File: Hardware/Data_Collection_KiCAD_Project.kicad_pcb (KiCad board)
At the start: 4 copper layers, 80 x 93.2 mm, 59 parts, among them IC1 STM32L562VET6Q, J1 10118192-0001LF, J2 Conn_Coaxial, J3 L717SDC37P1ACH4F, J4 I2C1 Debug, J6 UART Debug, J7 SPI 1 Debug, Q1 SI1040X-T1-GE3, U1 LM317T, U2 KX134-1211, U3 MCP9808_MSOP, U4 MAX-8Q, U5 USBLC6-2SC6, U6 W25Q32JVSS, U7 MS5607-02BA, U8 BNO055, Y1 32MHz, Y2 32.768kHz

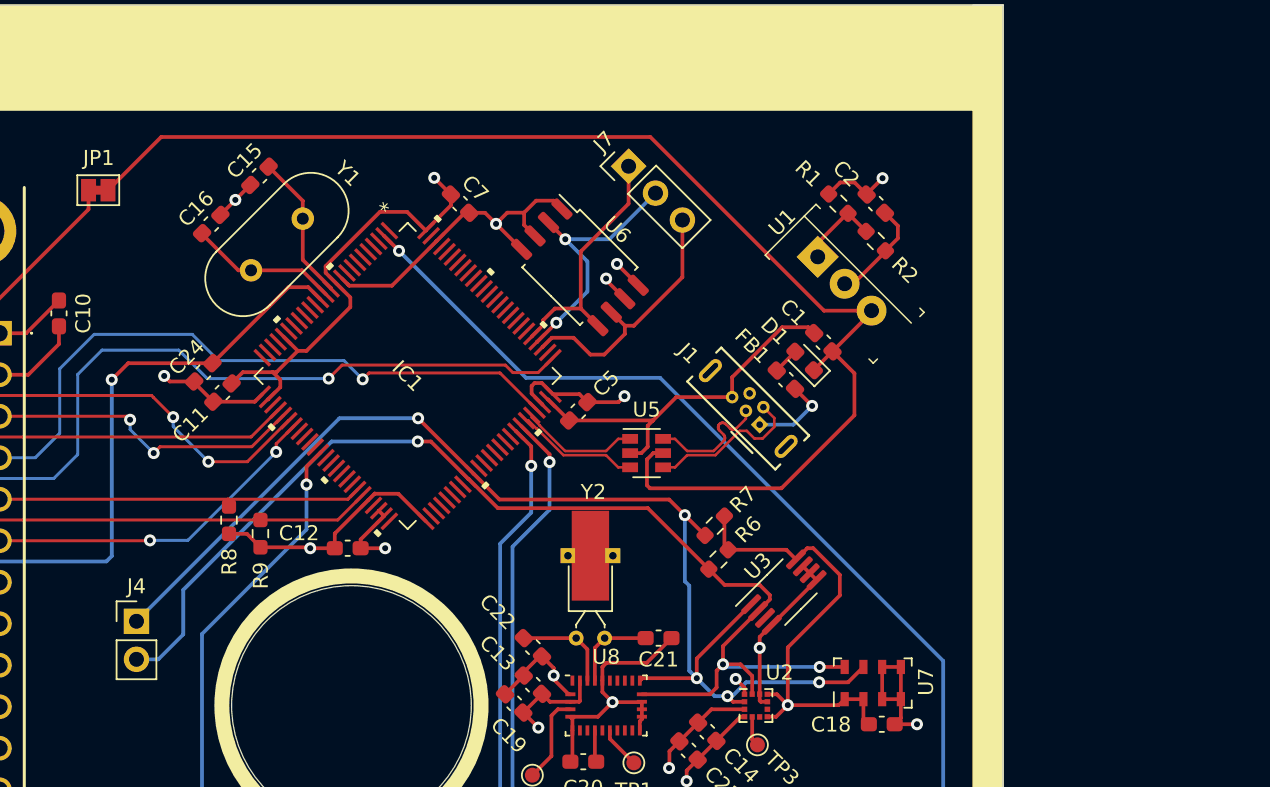
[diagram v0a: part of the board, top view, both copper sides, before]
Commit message: Updated MCU Component Sheet
Used the file from the Telemetry board for compatibility and commonality.
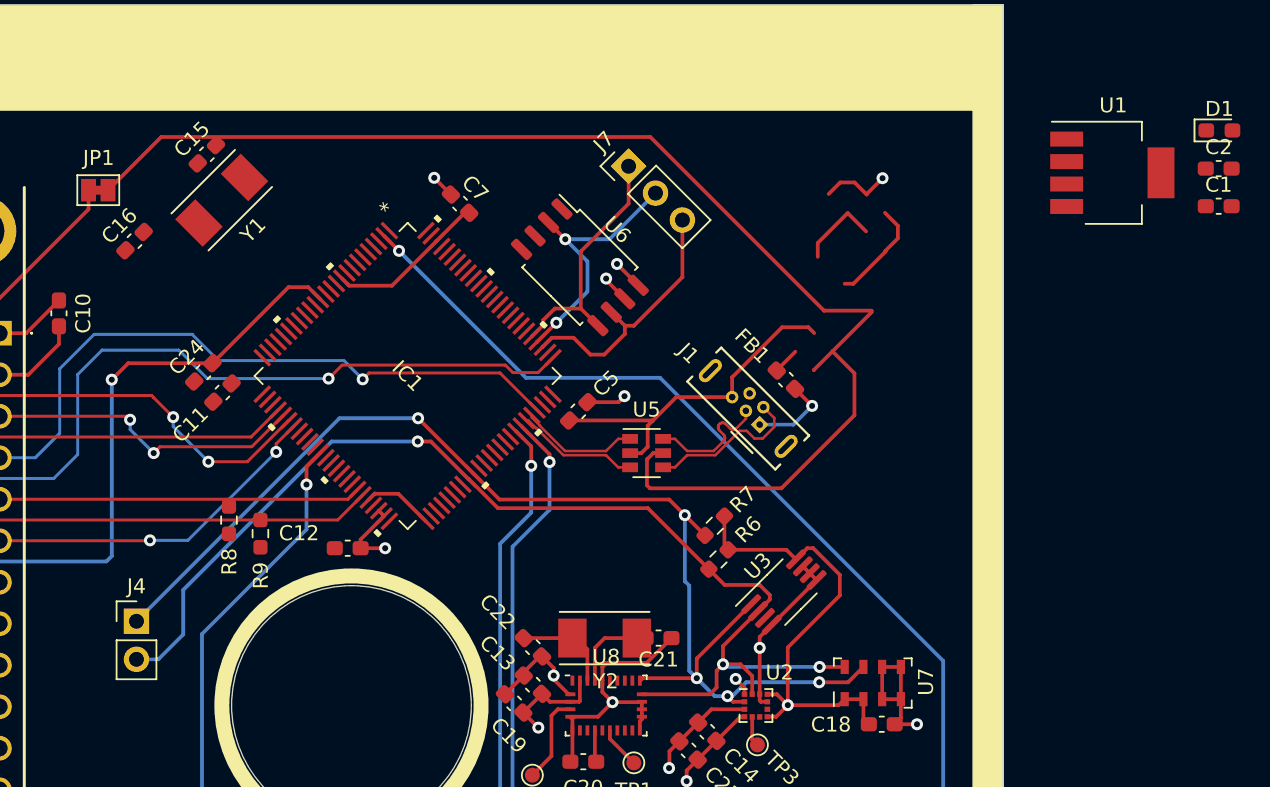
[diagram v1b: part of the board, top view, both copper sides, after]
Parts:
- removed R1: 390, Resistor_SMD:R_0603_1608Metric_Pad0.98x0.95mm_HandSolder
- removed R2: 240, Resistor_SMD:R_0603_1608Metric_Pad0.98x0.95mm_HandSolder
- D1: value D_Schottky -> D_Schottky_Small
- U1: value LM317T -> LP38692MPX-ADJ; footprint digikey-footprints:TO-220-3 -> Package_TO_SOT_SMD:SOT-223-5
- Y1: footprint Crystal:Crystal_HC49-4H_Vertical -> RDT_Custom_Footprints:XTAL_ABM7-32.000MHZ-D2Y-T
- Y2: footprint Crystal:Crystal_DS26_D2.0mm_L6.0mm_Horizontal_1EP_style2 -> RDT_Custom_Footprints:XTAL_ABM7-32.000MHZ-D2Y-T
- moved D1 31.7 mm to (174.4, 60.1), turned to 0 degrees
- moved C1 27.9 mm to (174.4, 65.1), turned to 0 degrees
- moved C2 23.0 mm to (174.4, 62.6), turned to 0 degrees
- moved U1 20.4 mm to (167.3, 62.9), turned to 0 degrees
- moved Y1 5.55 mm to (107.8, 64.7)
- moved C16 5.25 mm to (102.0, 67.5)
- moved C15 3.79 mm to (106.8, 61.7)
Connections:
- C2 pad 1: +3V3 -> Net-(C2-Pad1)
- IC1 pad 1: (no net) -> unconnected-(IC1-Pad1)
- IC1 pad 15: (no net) -> unconnected-(IC1-Pad15)
- IC1 pad 16: (no net) -> unconnected-(IC1-Pad16)
- IC1 pad 17: (no net) -> unconnected-(IC1-Pad17)
- IC1 pad 18: (no net) -> unconnected-(IC1-Pad18)
- IC1 pad 19: (no net) -> unconnected-(IC1-Pad19)
- IC1 pad 20: (no net) -> unconnected-(IC1-Pad20)
- IC1 pad 22: (no net) -> unconnected-(IC1-Pad22)
- IC1 pad 23: (no net) -> unconnected-(IC1-Pad23)
- IC1 pad 24: (no net) -> unconnected-(IC1-Pad24)
- IC1 pad 25: (no net) -> unconnected-(IC1-Pad25)
- IC1 pad 28: (no net) -> unconnected-(IC1-Pad28)
- IC1 pad 3: (no net) -> unconnected-(IC1-Pad3)
- IC1 pad 33: (no net) -> unconnected-(IC1-Pad33)
- IC1 pad 34: (no net) -> unconnected-(IC1-Pad34)
- IC1 pad 35: (no net) -> unconnected-(IC1-Pad35)
- IC1 pad 36: (no net) -> unconnected-(IC1-Pad36)
- IC1 pad 38: (no net) -> unconnected-(IC1-Pad38)
- IC1 pad 39: (no net) -> unconnected-(IC1-Pad39)
- IC1 pad 4: (no net) -> unconnected-(IC1-Pad4)
- IC1 pad 40: (no net) -> unconnected-(IC1-Pad40)
- IC1 pad 41: (no net) -> unconnected-(IC1-Pad41)
- IC1 pad 42: (no net) -> unconnected-(IC1-Pad42)
- IC1 pad 43: (no net) -> unconnected-(IC1-Pad43)
- IC1 pad 47: (no net) -> unconnected-(IC1-Pad47)
- IC1 pad 5: (no net) -> unconnected-(IC1-Pad5)
- IC1 pad 50: (no net) -> unconnected-(IC1-Pad50)
- IC1 pad 52: (no net) -> unconnected-(IC1-Pad52)
- IC1 pad 53: (no net) -> unconnected-(IC1-Pad53)
- IC1 pad 54: (no net) -> unconnected-(IC1-Pad54)
- IC1 pad 55: (no net) -> unconnected-(IC1-Pad55)
- IC1 pad 56: (no net) -> unconnected-(IC1-Pad56)
- IC1 pad 57: (no net) -> unconnected-(IC1-Pad57)
- IC1 pad 58: (no net) -> unconnected-(IC1-Pad58)
- IC1 pad 6: (no net) -> unconnected-(IC1-Pad6)
- IC1 pad 61: (no net) -> unconnected-(IC1-Pad61)
- IC1 pad 62: (no net) -> unconnected-(IC1-Pad62)
- IC1 pad 63: (no net) -> unconnected-(IC1-Pad63)
- IC1 pad 64: (no net) -> unconnected-(IC1-Pad64)
- IC1 pad 65: (no net) -> unconnected-(IC1-Pad65)
- IC1 pad 66: (no net) -> unconnected-(IC1-Pad66)
- IC1 pad 67: (no net) -> unconnected-(IC1-Pad67)
- IC1 pad 7: (no net) -> unconnected-(IC1-Pad7)
- IC1 pad 77: (no net) -> unconnected-(IC1-Pad77)
- IC1 pad 8: (no net) -> unconnected-(IC1-Pad8)
- IC1 pad 81: (no net) -> unconnected-(IC1-Pad81)
- IC1 pad 82: (no net) -> unconnected-(IC1-Pad82)
- IC1 pad 83: (no net) -> unconnected-(IC1-Pad83)
- IC1 pad 84: (no net) -> unconnected-(IC1-Pad84)
- IC1 pad 85: (no net) -> unconnected-(IC1-Pad85)
- IC1 pad 86: (no net) -> unconnected-(IC1-Pad86)
- IC1 pad 87: (no net) -> unconnected-(IC1-Pad87)
- IC1 pad 88: (no net) -> unconnected-(IC1-Pad88)
- IC1 pad 89: (no net) -> unconnected-(IC1-Pad89)
- IC1 pad 9: (no net) -> unconnected-(IC1-Pad9)
- IC1 pad 90: (no net) -> unconnected-(IC1-Pad90)
- IC1 pad 91: (no net) -> unconnected-(IC1-Pad91)
- IC1 pad 92: (no net) -> unconnected-(IC1-Pad92)
- IC1 pad 93: (no net) -> unconnected-(IC1-Pad93)
- IC1 pad 94: (no net) -> unconnected-(IC1-Pad94)
- IC1 pad 95: (no net) -> unconnected-(IC1-Pad95)
- IC1 pad 96: (no net) -> unconnected-(IC1-Pad96)
- IC1 pad 97: (no net) -> unconnected-(IC1-Pad97)
- IC1 pad 99: (no net) -> unconnected-(IC1-Pad99)
- J1 pad 4: (no net) -> unconnected-(J1-Pad4)
- J3 pad 10: (no net) -> unconnected-(J3-Pad10)
- J3 pad 11: (no net) -> unconnected-(J3-Pad11)
- J3 pad 12: (no net) -> unconnected-(J3-Pad12)
- J3 pad 13: (no net) -> unconnected-(J3-Pad13)
- J3 pad 14: (no net) -> unconnected-(J3-Pad14)
- J3 pad 15: (no net) -> unconnected-(J3-Pad15)
- J3 pad 16: (no net) -> unconnected-(J3-Pad16)
- J3 pad 17: (no net) -> unconnected-(J3-Pad17)
- J3 pad 26: (no net) -> /37 Pin DSUB Bus/Fire_redundant
- J3 pad 27: (no net) -> unconnected-(J3-Pad27)
- J3 pad 28: (no net) -> unconnected-(J3-Pad28)
- J3 pad 29: (no net) -> unconnected-(J3-Pad29)
- J3 pad 30: (no net) -> unconnected-(J3-Pad30)
- J3 pad 31: (no net) -> unconnected-(J3-Pad31)
- J3 pad 32: (no net) -> unconnected-(J3-Pad32)
- J3 pad 33: (no net) -> unconnected-(J3-Pad33)
- J3 pad 34: (no net) -> unconnected-(J3-Pad34)
- J3 pad 35: (no net) -> unconnected-(J3-Pad35)
- J3 pad 36: (no net) -> unconnected-(J3-Pad36)
- J3 pad 7: (no net) -> /37 Pin DSUB Bus/Fire
- J3 pad 8: (no net) -> unconnected-(J3-Pad8)
- J3 pad 9: (no net) -> unconnected-(J3-Pad9)
- U1 pad 1: Net-(R1-Pad1) -> GND
- U1 pad 2: +3V3 -> +5V
- U2 pad 6: (no net) -> /KX134-1211/KX134_INT2
- U3 pad 3: (no net) -> /MCP9808/ALERT
- U4 pad 15: (no net) -> unconnected-(U4-Pad15)
- U4 pad 18: (no net) -> unconnected-(U4-Pad18)
- U4 pad 4: (no net) -> unconnected-(U4-Pad4)
- U4 pad 9: (no net) -> /MAX-8Q/~{RESET}
- U8 pad 1: (no net) -> unconnected-(U8-Pad1)
- U8 pad 10: (no net) -> /BNO055/BNO055_BTL_IND
- U8 pad 12: (no net) -> unconnected-(U8-Pad12)
- U8 pad 13: (no net) -> unconnected-(U8-Pad13)
- U8 pad 14: (no net) -> /BNO055/BNO055_INT
- U8 pad 21: (no net) -> unconnected-(U8-Pad21)
- U8 pad 22: (no net) -> unconnected-(U8-Pad22)
- U8 pad 23: (no net) -> unconnected-(U8-Pad23)
- U8 pad 24: (no net) -> unconnected-(U8-Pad24)
- U8 pad 7: (no net) -> unconnected-(U8-Pad7)
- U8 pad 8: (no net) -> unconnected-(U8-Pad8)
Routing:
- net +3V3: track 124.8 -> 78.3 mm, vias 8 -> 7
- net GND: track 184.7 -> 160.7 mm, vias 14 -> 11
- net Net-(C16-Pad1): track 9.98 -> 0.00 mm
- net Net-(C15-Pad1): track 9.89 -> 0.00 mm
- net /EXT_SCL: track 24.7 -> 24.2 mm

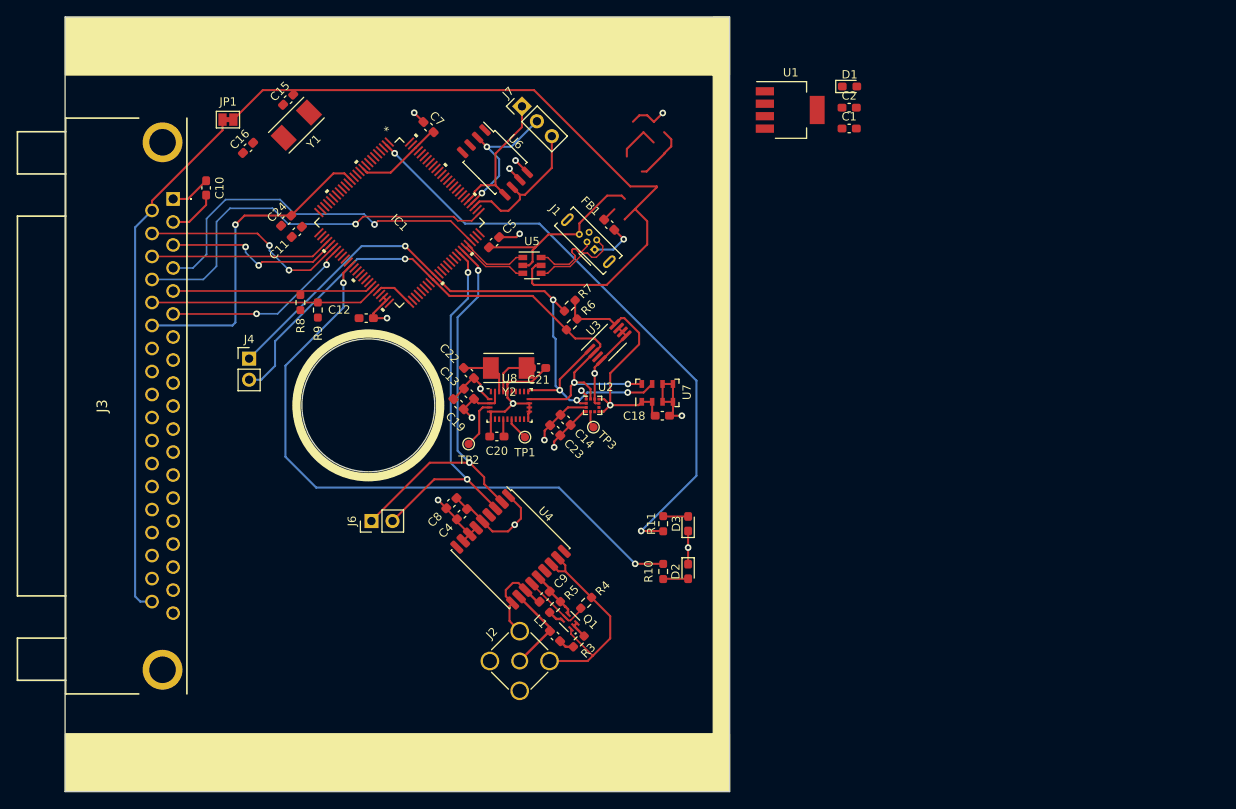
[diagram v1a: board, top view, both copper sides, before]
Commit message: Organized components, arranged filter caps
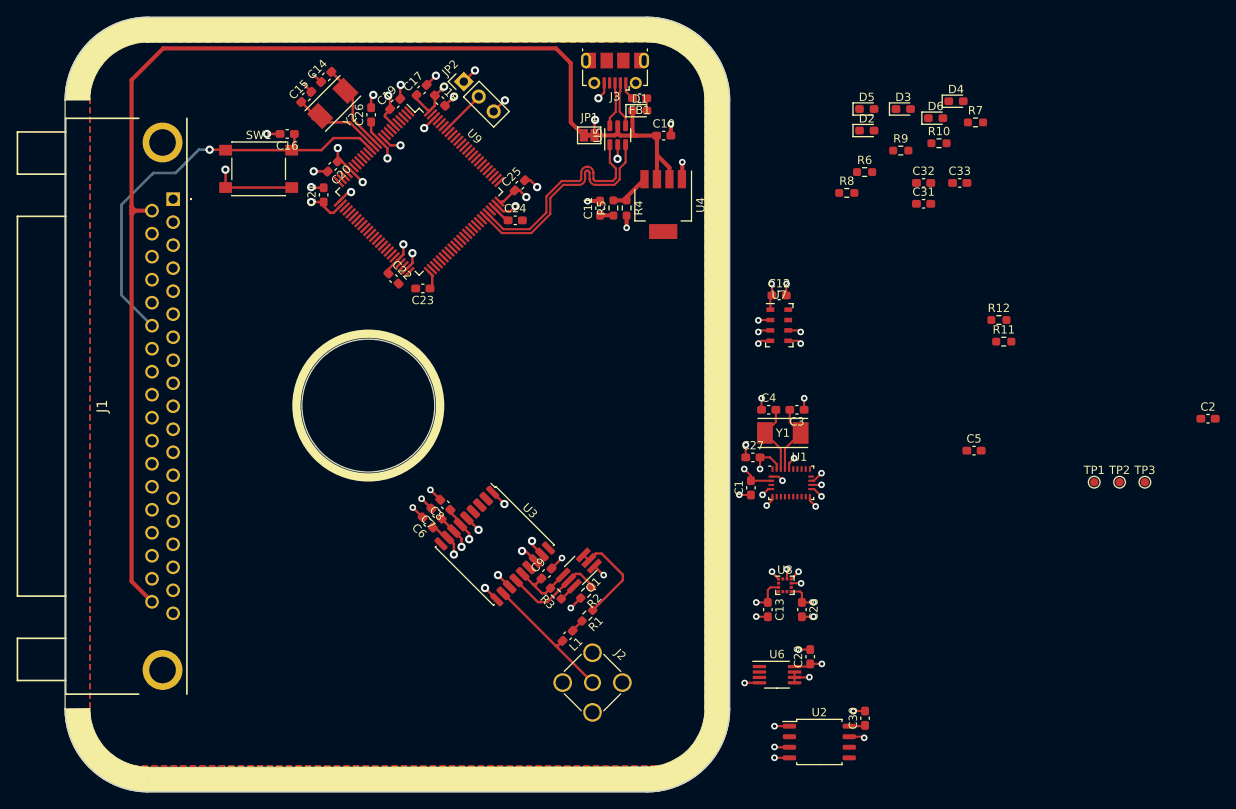
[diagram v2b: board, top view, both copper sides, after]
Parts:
- removed IC1: STM32L562VET6Q, STM32L562VET6Q:STM32L562VET6Q
- removed J4: I2C1 Debug, Connector_PinHeader_2.54mm:PinHeader_1x02_P2.54mm_Vertical
- removed J6: UART Debug, Connector_PinHeader_2.54mm:PinHeader_1x02_P2.54mm_Vertical
- removed J7: SPI 1 Debug, Connector_PinHeader_2.54mm:PinHeader_1x03_P2.54mm_Vertical
- added C17: 1uF, Capacitor_SMD:C_0603_1608Metric_Pad1.08x0.95mm_HandSolder, F.Cu at (122.9, 60.5)
- added C25: 100nF, Capacitor_SMD:C_0603_1608Metric_Pad1.08x0.95mm_HandSolder, F.Cu at (134.7, 72.0)
- added C26: 100nF, Capacitor_SMD:C_0603_1608Metric_Pad1.08x0.95mm_HandSolder, F.Cu at (116.8, 63.5)
- added C27: 0.1uF, Capacitor_SMD:C_0603_1608Metric_Pad1.08x0.95mm_HandSolder, F.Cu at (162.8, 104.7)
- added C28: 0.1uF, Capacitor_SMD:C_0603_1608Metric_Pad1.08x0.95mm_HandSolder, F.Cu at (168.7, 123.1)
- added C29: 0.1uF, Capacitor_SMD:C_0603_1608Metric_Pad1.08x0.95mm_HandSolder, F.Cu at (169.7, 128.7)
- added C3: 0.1uF, Capacitor_SMD:C_0603_1608Metric_Pad1.08x0.95mm_HandSolder, F.Cu at (168.1, 99.0)
- added C30: 0.1uF, Capacitor_SMD:C_0603_1608Metric_Pad1.08x0.95mm_HandSolder, F.Cu at (176.3, 136.1)
- added C31: 0.1uF, Capacitor_SMD:C_0603_1608Metric_Pad1.08x0.95mm_HandSolder, F.Cu at (183.3, 74.2)
- added C32: 0.1uF, Capacitor_SMD:C_0603_1608Metric_Pad1.08x0.95mm_HandSolder, F.Cu at (183.3, 71.7)
- added C33: 0.1uF, Capacitor_SMD:C_0603_1608Metric_Pad1.08x0.95mm_HandSolder, F.Cu at (187.7, 71.7)
- added C6: 100nF, Capacitor_SMD:C_0603_1608Metric_Pad1.08x0.95mm_HandSolder, F.Cu at (123.6, 112.6)
- added D4: Red, LED_SMD:LED_0603_1608Metric_Pad1.05x0.95mm_HandSolder, F.Cu at (187.2, 61.9)
- added D5: Grn, LED_SMD:LED_0603_1608Metric_Pad1.05x0.95mm_HandSolder, F.Cu at (176.5, 62.8)
- added D6: Red, LED_SMD:LED_0603_1608Metric_Pad1.05x0.95mm_HandSolder, F.Cu at (184.8, 63.9)
- added JP2: Debug Jumper, Connector_PinHeader_2.54mm:PinHeader_1x03_P2.54mm_Vertical, F.Cu at (128.0, 59.5)
- added R1: 10k, Resistor_SMD:R_0603_1608Metric_Pad0.98x0.95mm_HandSolder, F.Cu at (142.9, 123.8)
- added R12: 4.7k, Resistor_SMD:R_0603_1608Metric_Pad0.98x0.95mm_HandSolder, F.Cu at (192.4, 88.2)
- added R2: 10k, Resistor_SMD:R_0603_1608Metric_Pad0.98x0.95mm_HandSolder, F.Cu at (142.7, 121.0)
- added SW1: MCU Reset, Button_Switch_SMD:SW_SPST_PTS645, F.Cu at (103.3, 70.0)
- added U9: STM32L562VET6Q, Package_QFP:LQFP-100_14x14mm_P0.5mm, F.Cu at (122.6, 72.8)
- C10, C2, C4: value 1uF -> 0.1uF
- C11, C5: value 100nF -> 1uF
- C13: value 100nF -> 0.1uF
- C14: value 100nF -> 30pF
- C16: value 30pF -> 100nF
- C19, C20, C21, C22, C23: value 0.1uF -> 100nF
- D2: value Green -> Red; footprint Diode_SMD:D_0603_1608Metric_Pad1.05x0.95mm_HandSolder -> LED_SMD:LED_0603_1608Metric_Pad1.05x0.95mm_HandSolder
- D3: value Red -> Grn; footprint Diode_SMD:D_0603_1608Metric_Pad1.05x0.95mm_HandSolder -> LED_SMD:LED_0603_1608Metric_Pad1.05x0.95mm_HandSolder
- J1: value 10118192-0001LF -> L717SDC37P1ACH4F; footprint Connector_USB:USB_Micro-B_Wuerth_614105150721_Vertical -> RDT_Custom_Footprints:L717SDC37P1ACH4F
- J3: value L717SDC37P1ACH4F -> 10118192-0001LF; footprint RDT_Custom_Footprints:L717SDC37P1ACH4F -> Connector_USB:USB_Micro-B_Molex-105017-0001
- Q1: footprint SC-89:SC-89 -> Package_TO_SOT_SMD:TSOT-23-6_HandSoldering
- R10: value 80 -> 820
- R11: value 80 -> 4.7k
- R3: value 10k -> 100k
- R4: value 10k -> 390
- R5: value 100k -> 240
- R6, R7: value 4.7K -> 820
- R8, R9: value DNP -> 820
- U1: value LP38692MPX-ADJ -> BNO055; footprint Package_TO_SOT_SMD:SOT-223-5 -> Package_LGA:LGA-28_5.2x3.8mm_P0.5mm
- U2: value KX134-1211 -> W25Q32JVSS; footprint Package_LGA:LGA-12_2x2mm_P0.5mm -> Package_SO:SOIC-8_5.23x5.23mm_P1.27mm
- U3: value MCP9808_MSOP -> MAX-8Q; footprint Package_SO:MSOP-8_3x3mm_P0.65mm -> RF_GPS:ublox_MAX
- U4: value MAX-8Q -> LP38692MPX-ADJ; footprint RF_GPS:ublox_MAX -> Package_TO_SOT_SMD:SOT-223-5
- U6: value W25Q32JVSS -> MCP9808_MSOP; footprint Package_SO:SOIC-8_5.23x5.23mm_P1.27mm -> Package_SO:MSOP-8_3x3mm_P0.65mm
- U8: value BNO055 -> KX134-1211; footprint Package_LGA:LGA-28_5.2x3.8mm_P0.5mm -> Package_LGA:LGA-12_2x2mm_P0.5mm
- Y1: value 32MHz -> 32.768kHz
- Y2: value 32.768kHz -> 32MHz
- moved TP2 78.5 mm to (206.9, 107.7)
- moved R9 72.8 mm to (180.6, 67.8), turned to 0 degrees
- moved U6 70.4 mm to (165.7, 130.9), turned to 0 degrees
- moved Y1 69.3 mm to (166.4, 101.8), turned to 180 degrees
- moved TP1 68.8 mm to (203.9, 107.7)
- moved R8 67.1 mm to (174.1, 72.9), turned to 0 degrees
- moved TP3 66.7 mm to (210.0, 107.7)
- moved C5 63.0 mm to (189.4, 103.9), turned to 0 degrees
- moved R10 61.3 mm to (185.2, 66.9), turned to 0 degrees
- moved D2 57.3 mm to (176.5, 65.4), turned to 0 degrees
- moved C2 57.2 mm to (217.6, 100.1)
- moved D3 56.2 mm to (180.9, 62.8), turned to 0 degrees
- moved C10 55.4 mm to (152.1, 66.0), turned to 0 degrees
- moved J3 55.4 mm to (146.2, 58.2), turned to 180 degrees
- moved R7 53.6 mm to (189.6, 64.4), turned to 0 degrees
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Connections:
- C1 pad 1: +5V -> GND
- C1 pad 2: GND -> +3V3
- C10 pad 1: +3V3 -> +5V
- C11 pad 1: +3V3 -> Net-(C11-Pad1)
- C14 pad 1: +3V3 -> Net-(C14-Pad1)
- C16 pad 1: Net-(C16-Pad1) -> /NRST
- C19 pad 1: GND -> +3V3
- C19 pad 2: +3V3 -> GND
- C2 pad 1: Net-(C2-Pad1) -> GND
- C2 pad 2: GND -> Net-(C2-Pad2)
- C20 pad 1: GND -> +3V3
- C20 pad 2: Net-(C20-Pad2) -> GND
- C21 pad 1: GND -> +3V3
- C21 pad 2: Net-(C21-Pad2) -> GND
- C22 pad 1: GND -> +3V3
- C22 pad 2: Net-(C22-Pad2) -> GND
- C23 pad 1: GND -> +3V3
- C23 pad 2: +3V3 -> GND
- C24 pad 1: /NRST -> +3V3
- C4 pad 1: +3V3 -> GND
- C4 pad 2: GND -> Net-(C4-Pad2)
- D2 pad 1: GND -> Net-(D2-Pad1)
- D3 pad 1: GND -> Net-(D3-Pad1)
- J1 pad 1: Net-(FB1-Pad2) -> GND
- J1 pad 2: /USB Connector and ESD/USB_CONN_D- -> +3V3
- J1 pad 3: /USB Connector and ESD/USB_CONN_D+ -> /TELEMETRY_MISO
- J1 pad 4: unconnected-(J1-Pad4) -> /SWDIO
- J1 pad 5: GND -> /ALERT_SCL
- J1 pad 6: (no net) -> /ALERT_EN
- J3 pad 1: GND -> Net-(FB1-Pad2)
- J3 pad 2: +3V3 -> /USB Connector and ESD/USB_CONN_D-
- J3 pad 3: /SPI2_MISO -> /USB Connector and ESD/USB_CONN_D+
- J3 pad 4: /SWDIO -> unconnected-(J3-Pad4)
- J3 pad 5: /EXT_SCL -> GND
- J3 pad 6: /I2C_ALERT -> (no net)
- R10 pad 1: Net-(IC1-Pad37) -> GND
- R10 pad 2: Net-(D2-Pad2) -> Net-(D6-Pad1)
- R11 pad 1: Net-(IC1-Pad2) -> /SENSOR_SCL
- R11 pad 2: Net-(D3-Pad2) -> +3V3
- R3 pad 1: Net-(Q1-Pad2) -> Net-(Q1-Pad6)
- R3 pad 2: Net-(L1-Pad1) -> /MAX-8Q/GPS_VCC_RF
- R4 pad 1: /MAX-8Q/GPS_LNA_EN -> Net-(R4-Pad1)
- R5 pad 1: Net-(Q1-Pad6) -> Net-(C11-Pad1)
- R5 pad 2: /MAX-8Q/GPS_VCC_RF -> Net-(R4-Pad1)
- R6 pad 1: /I2C1_SCL -> GND
- R6 pad 2: +3V3 -> Net-(D2-Pad1)
- R7 pad 1: /I2C1_SDA -> GND
- R7 pad 2: +3V3 -> Net-(D3-Pad1)
- R8 pad 1: /EXT_SCL -> GND
- R8 pad 2: +3V3 -> Net-(D4-Pad1)
- R9 pad 1: /EXT_SDA -> GND
- R9 pad 2: +3V3 -> Net-(D5-Pad1)
- U1 pad 1: GND -> unconnected-(U1-Pad1)
- U1 pad 2: +5V -> GND
- U1 pad 3: +5V -> +3V3
- U1 pad 4: Net-(R1-Pad1) -> /BNO055/~{BNO055_BTL}
- U1 pad 5: +3V3 -> GND
- U2 pad 2: /I2C1_SDA -> /FLASH_MISO
- U2 pad 3: +3V3 -> GND
- U2 pad 5: /KX134-1211/KX134_INT1 -> /FLASH_MOSI
- U2 pad 6: /KX134-1211/KX134_INT2 -> /FLASH_CLK
- U2 pad 7: +3V3 -> GND
- U2 pad 8: (no net) -> +3V3
- U3 pad 1: /I2C1_SDA -> GND
- U3 pad 2: /I2C1_SCL -> /GPS_TX
- U3 pad 3: /MCP9808/ALERT -> /GPS_RX
- U3 pad 4: GND -> unconnected-(U3-Pad4)
- U3 pad 6: GND -> +3V3
- U3 pad 7: GND -> +3V3
- U4 pad 2: /USART1_RX -> +5V
- U4 pad 3: /USART1_TX -> +5V
- U4 pad 4: unconnected-(U4-Pad4) -> Net-(R4-Pad1)
- U4 pad 5: GND -> +3V3
- U6 pad 1: GND -> /SENSOR_SDA
- U6 pad 2: /SPI1_MISO -> /SENSOR_SCL
- U6 pad 3: GND -> /MCP9808/ALERT
- U6 pad 5: /SPI1_MOSI -> GND
- U6 pad 6: /SPI1_SCK -> GND
- U7 pad 7: /I2C1_SDA -> /SENSOR_SDA
- U7 pad 8: /I2C1_SCL -> /SENSOR_SCL
- U8 pad 1: unconnected-(U8-Pad1) -> GND
- U8 pad 10: /BNO055/BNO055_BTL_IND -> +3V3
- U8 pad 11: /BNO055/~{BNO055_RESET} -> GND
- U8 pad 12: unconnected-(U8-Pad12) -> /SENSOR_SCL
- U8 pad 2: GND -> /SENSOR_SDA
- U8 pad 4: /BNO055/~{BNO055_BTL} -> GND
- U8 pad 5: GND -> /KX134-1211/KX134_INT1
- U8 pad 6: GND -> /KX134-1211/KX134_INT2
- U8 pad 7: unconnected-(U8-Pad7) -> +3V3
- U8 pad 8: unconnected-(U8-Pad8) -> (no net)
- U8 pad 9: Net-(C20-Pad2) -> GND
- Y1 pad 1: Net-(C15-Pad1) -> Net-(C3-Pad2)
- Y1 pad 2: Net-(C16-Pad1) -> Net-(C4-Pad2)
- Y2 pad 1: Net-(C21-Pad2) -> Net-(C14-Pad1)
- Y2 pad 2: Net-(C22-Pad2) -> Net-(C15-Pad1)
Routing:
- net /I2C1_SDA: track 82.3 -> 0.00 mm, vias 5 -> 0
- net /I2C1_SCL: track 78.8 -> 0.00 mm, vias 3 -> 0
- net Net-(IC1-Pad37): track 77.2 -> 0.00 mm, vias 2 -> 0
- net Net-(IC1-Pad2): track 72.6 -> 0.00 mm, vias 2 -> 0
- net /37 Pin DSUB Bus/Dsub_5v: track 64.1 -> 132.1 mm
- net +5V: track 86.6 -> 23.3 mm, vias 0 -> 1
- net /USART1_RX: track 49.4 -> 0.00 mm, vias 2 -> 0
- net /SWCLK: track 48.0 -> 0.00 mm, vias 1 -> 0
- net /USART1_TX: track 45.5 -> 0.00 mm, vias 2 -> 0
- net /SWDIO: track 44.3 -> 0.00 mm, vias 1 -> 0
- net GND: track 160.7 -> 118.0 mm, vias 11 -> 65
- net /EXT_SDA: track 27.5 -> 0.00 mm
- net /SPI2_MOSI: track 25.2 -> 0.00 mm, vias 2 -> 0
- net /EXT_SCL: track 24.2 -> 0.00 mm
- net /I2C_ALERT: track 23.2 -> 0.00 mm, vias 2 -> 0
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- added copper zone on B.Cu, net GND
- added copper zone on F.Cu, net GND
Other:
- board size 80 x 93.2 mm -> 80 x 93.3 mm
- board text added: "100nF"
- board text added: "U4"

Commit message: Added silkscreen art
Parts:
- added G***: LOGO, RDT_Graphics:Data_Collection_QRCode, B.Cu at (121.8, 132.1)
- added G***: LOGO, Custom_Graphics:RDT_Logo, B.Cu at (102.6, 98.5)

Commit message: Added signatures to silkscreen
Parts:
- added G***: LOGO, Custom_Graphics:ThomasFSignature, B.Cu at (120.0, 60.7)
- added G***: LOGO, RDT_Graphics:SethSSignature, B.Cu at (120.0, 134.3)
- moved G*** 42.3 mm to (147.5, 98.5)
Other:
- board text added: "Seth Sievers"
- board text added: "Thomas Francois KXØSTL"
